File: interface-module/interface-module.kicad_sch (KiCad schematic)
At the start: 11 parts, among them J2 Conn_01x02, J4 Conn_01x08, J6 Conn_01x08, SW1 SW_Coded_SH-7050

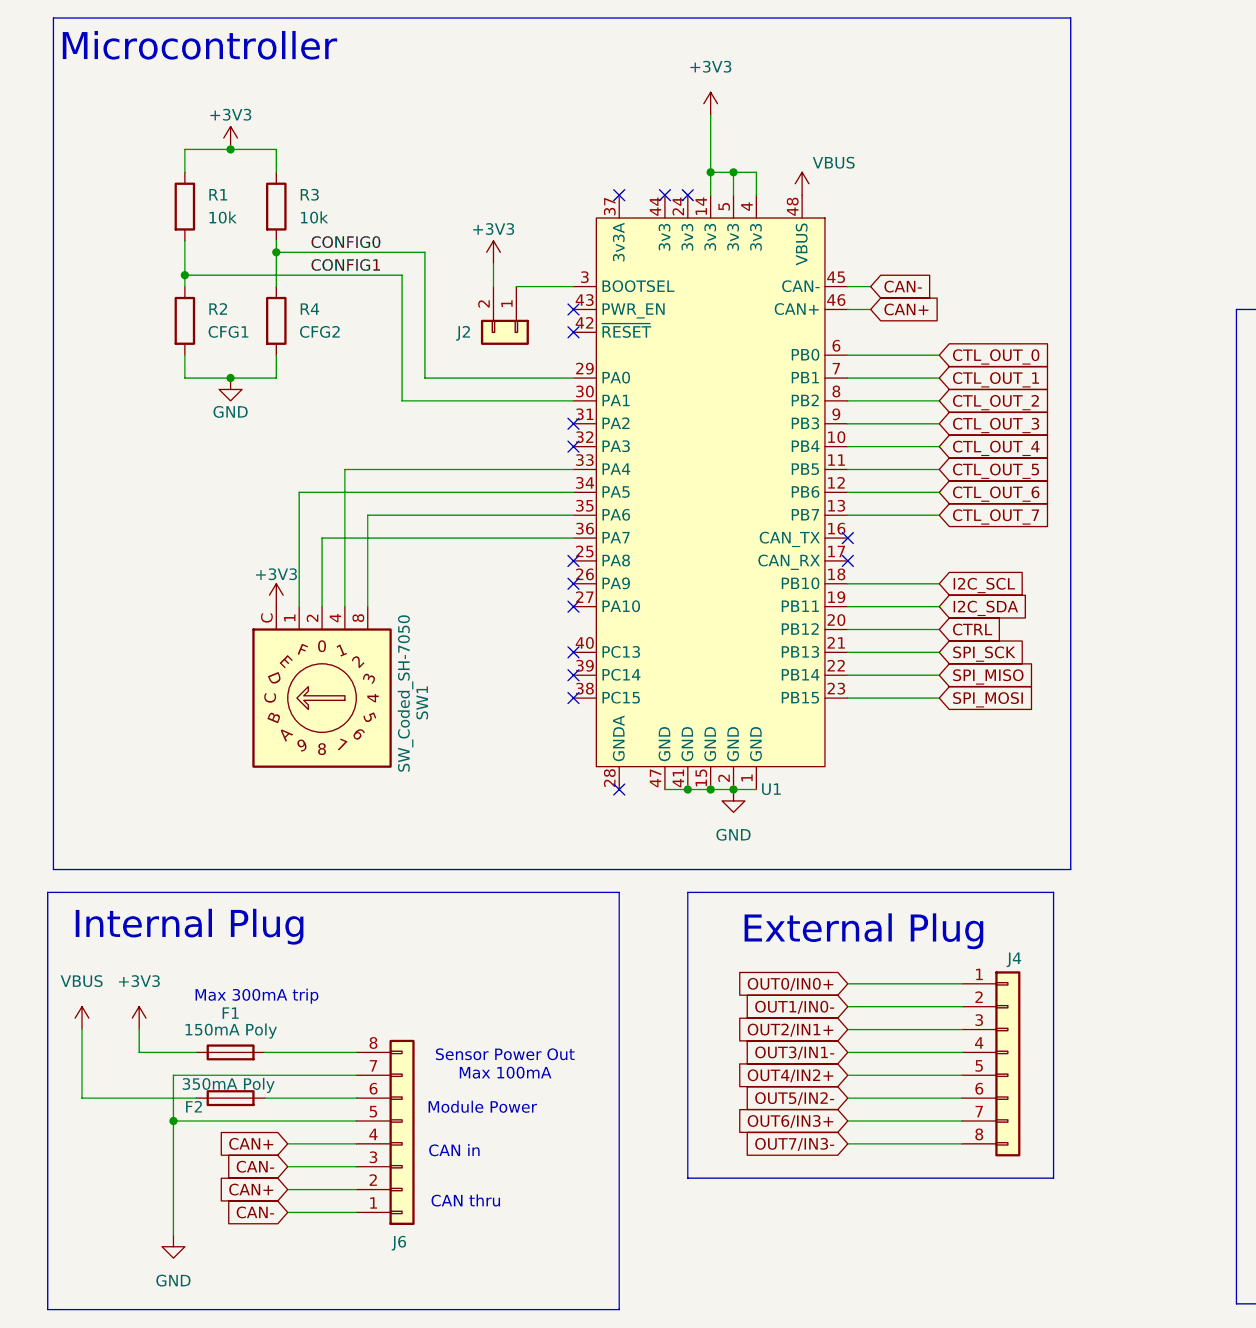
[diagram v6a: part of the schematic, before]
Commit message: Added LEDs for outputs and improved silkscreen
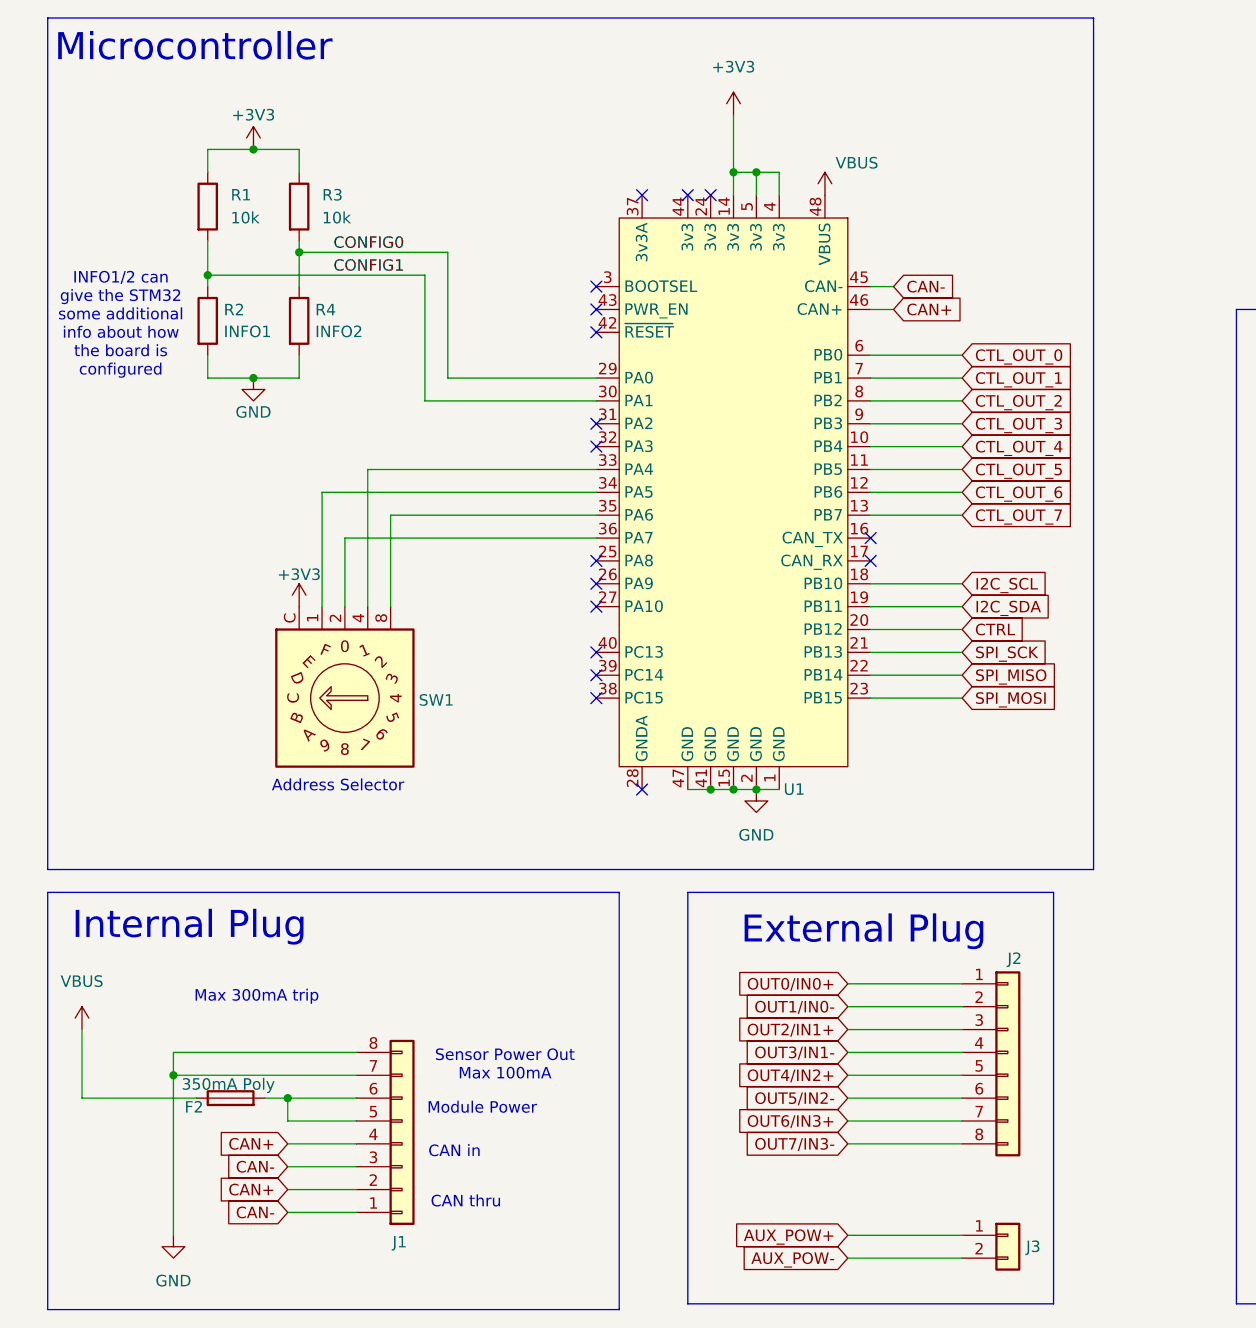
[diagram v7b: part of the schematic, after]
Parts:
- removed F1: 150mA Poly, Fuse:Fuse_1206_3216Metric, symbol Device:Fuse
- removed J2: Conn_01x02, TestPoint:TestPoint_2Pads_Pitch2.54mm_Drill0.8mm, symbol Connector_Generic:Conn_01x02
- added J3: Conn_01x02, TerminalBlock:TerminalBlock_bornier-2_P5.08mm, symbol Connector_Generic:Conn_01x02
- R2: value CFG1 -> INFO1
- R4: value CFG2 -> INFO2
- renumbered J6 to J1, J4 to J2
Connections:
- net GND: now also J1.8 (Pin_8); no longer J1.5 (Pin_5)
- net at F2.2, J1.6 (Pin_6): now also J1.5 (Pin_5)
- new net AUX_POW+: J3.1 (Pin_1)
- new net AUX_POW-: J3.2 (Pin_2)
- no-connect marks 16 -> 17
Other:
- note added: "Address Selector"
- note added: "INFO1/2 can give the STM32 some additional info about how the board is configured"
- moved on the sheet: R1, R2, R3, R4, SW1, U1

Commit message: Fixed BOM issues
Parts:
- R1, R3: MPN RMCF0603FT10K0 -> RMCF0603FT10K0
- U1: now left out of the parts list
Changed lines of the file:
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@@
 			)
 		)
-		(property "MPN" "RMCF0603FT10K0 "
+		(property "MPN" "RMCF0603FT10K0"
 			(at 36.83 41.91 0)
 			(effects
@@
 		(unit 1)
 		(exclude_from_sim no)
-		(in_bom yes)
+		(in_bom no)
 		(on_board yes)
 		(dnp no)
@@
 			)
 		)
-		(property "MPN" "RMCF0603FT10K0 "
+		(property "MPN" "RMCF0603FT10K0"
 			(at 46.99 41.91 0)
 			(effects
